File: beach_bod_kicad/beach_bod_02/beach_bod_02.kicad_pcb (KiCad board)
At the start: 2 copper layers, 78.2 x 29.2 mm, 86 parts, among them J1 Conn_01x01, J3 BNC5-J-P-GN-RA-BH2D, J4 Conn_01x01, J5 USB4085-GF-A_REVA4, J6 USB4085-GF-A_REVA4, Q1 AO3401A, U1 LTC6269, U2 LTC6268, U3 LM7301_SOT23_5

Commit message: Routed beach_bod_02
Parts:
- removed the C18 at (152.7, 113.0)
- removed the C19 at (148.7, 113.0)
- removed the C20 at (144.8, 113.0)
- removed the C21 at (140.8, 113.0)
- removed the R15 at (152.8, 109.6)
- removed the R16 at (148.8, 109.6)
- removed the R17 at (144.8, 109.6)
- removed the R18 at (140.9, 109.6)
- removed the R9 at (115.0, 55.8)
- removed the REF** at (150.9, 91.2) (x2)
- C1: renamed from C2; footprint Capacitor_SMD:C_0805_2012Metric_Pad1.18x1.45mm_HandSolder -> Capacitor_SMD:C_0603_1608Metric_Pad1.08x0.95mm_HandSolder
- C12: renamed from C8; footprint Capacitor_SMD:C_0805_2012Metric_Pad1.18x1.45mm_HandSolder -> Capacitor_SMD:C_0603_1608Metric_Pad1.08x0.95mm_HandSolder
- C13: renamed from C9; footprint Capacitor_SMD:C_0805_2012Metric_Pad1.18x1.45mm_HandSolder -> Capacitor_SMD:C_0603_1608Metric_Pad1.08x0.95mm_HandSolder
- C15: renamed from C13; footprint Capacitor_SMD:C_0805_2012Metric_Pad1.18x1.45mm_HandSolder -> Capacitor_SMD:C_0603_1608Metric_Pad1.08x0.95mm_HandSolder
- C16: renamed from C14; footprint Capacitor_SMD:C_0805_2012Metric_Pad1.18x1.45mm_HandSolder -> Capacitor_SMD:C_0603_1608Metric_Pad1.08x0.95mm_HandSolder
- C2: renamed from C3; footprint Capacitor_SMD:C_0805_2012Metric_Pad1.18x1.45mm_HandSolder -> Capacitor_SMD:C_0603_1608Metric_Pad1.08x0.95mm_HandSolder
- C3: renamed from C4; footprint Capacitor_SMD:C_0805_2012Metric_Pad1.18x1.45mm_HandSolder -> Capacitor_SMD:C_0603_1608Metric_Pad1.08x0.95mm_HandSolder
- C32: renamed from C34; footprint Capacitor_SMD:C_1210_3225Metric_Pad1.33x2.70mm_HandSolder -> Capacitor_SMD:C_0603_1608Metric_Pad1.08x0.95mm_HandSolder
- C4: renamed from C5; footprint Capacitor_SMD:C_0805_2012Metric_Pad1.18x1.45mm_HandSolder -> Capacitor_SMD:C_0603_1608Metric_Pad1.08x0.95mm_HandSolder
- C5: renamed from C18; footprint Capacitor_SMD:C_0805_2012Metric_Pad1.18x1.45mm_HandSolder -> Capacitor_SMD:C_0603_1608Metric_Pad1.08x0.95mm_HandSolder
- C6: renamed from C19; footprint Capacitor_SMD:C_0805_2012Metric_Pad1.18x1.45mm_HandSolder -> Capacitor_SMD:C_0603_1608Metric_Pad1.08x0.95mm_HandSolder
- C7: renamed from C20; footprint Capacitor_SMD:C_0805_2012Metric_Pad1.18x1.45mm_HandSolder -> Capacitor_SMD:C_0603_1608Metric_Pad1.08x0.95mm_HandSolder
- C8: renamed from C21; footprint Capacitor_SMD:C_0805_2012Metric_Pad1.18x1.45mm_HandSolder -> Capacitor_SMD:C_0603_1608Metric_Pad1.08x0.95mm_HandSolder
- R1: renamed from R3; footprint Resistor_SMD:R_0805_2012Metric_Pad1.20x1.40mm_HandSolder -> Resistor_SMD:R_0603_1608Metric_Pad0.98x0.95mm_HandSolder
- R10: renamed from R18; footprint Resistor_SMD:R_0805_2012Metric_Pad1.20x1.40mm_HandSolder -> Resistor_SMD:R_0603_1608Metric_Pad0.98x0.95mm_HandSolder
- R2: renamed from R4; footprint Resistor_SMD:R_0805_2012Metric_Pad1.20x1.40mm_HandSolder -> Resistor_SMD:R_0603_1608Metric_Pad0.98x0.95mm_HandSolder
- R3: renamed from R5; footprint Resistor_SMD:R_0805_2012Metric_Pad1.20x1.40mm_HandSolder -> Resistor_SMD:R_0603_1608Metric_Pad0.98x0.95mm_HandSolder
- R4: renamed from R6; footprint Resistor_SMD:R_0805_2012Metric_Pad1.20x1.40mm_HandSolder -> Resistor_SMD:R_0603_1608Metric_Pad0.98x0.95mm_HandSolder
- R5: renamed from R8; footprint Resistor_SMD:R_0805_2012Metric_Pad1.20x1.40mm_HandSolder -> Resistor_SMD:R_0603_1608Metric_Pad0.98x0.95mm_HandSolder
- R6: renamed from R13; footprint Resistor_SMD:R_0805_2012Metric_Pad1.20x1.40mm_HandSolder -> Resistor_SMD:R_0603_1608Metric_Pad0.98x0.95mm_HandSolder
- R7: renamed from R15; footprint Resistor_SMD:R_0805_2012Metric_Pad1.20x1.40mm_HandSolder -> Resistor_SMD:R_0603_1608Metric_Pad0.98x0.95mm_HandSolder
- R8: renamed from R16; footprint Resistor_SMD:R_0805_2012Metric_Pad1.20x1.40mm_HandSolder -> Resistor_SMD:R_0603_1608Metric_Pad0.98x0.95mm_HandSolder
- R9: renamed from R17; footprint Resistor_SMD:R_0805_2012Metric_Pad1.20x1.40mm_HandSolder -> Resistor_SMD:R_0603_1608Metric_Pad0.98x0.95mm_HandSolder
- moved C17 57.8 mm to (115.1, 99.9), turned to 90 degrees
- moved U2 52.0 mm to (115.4, 95.5), turned to 90 degrees
- moved C18 50.7 mm to (116.8, 100.0), turned to 90 degrees
- moved D1 50.3 mm to (141.2, 91.4), turned to -90 degrees
- moved R17 48.8 mm to (120.4, 97.3)
- moved R18 48.6 mm to (110.8, 98.4), turned to 90 degrees
- moved C19 48.3 mm to (112.9, 98.6), turned to 90 degrees
- moved R21 46.4 mm to (126.5, 102.1), turned to 0 degrees
- moved C14 46.2 mm to (127.7, 92.2)
- moved D2 46.2 mm to (141.2, 100.4), turned to 90 degrees
- moved C11 45.4 mm to (112.0, 95.0), turned to 0 degrees
- moved R19 44.4 mm to (134.4, 99.3)
- moved C21 44.4 mm to (121.8, 94.0)
- moved R20 44.3 mm to (122.2, 100.8), turned to 0 degrees
- moved R11 44.3 mm to (134.4, 92.5)
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- renumbered C6 to C10, C7 to C11, C12 to C14, C16 to C17, C17 to C18, C22 to C19, C23 to C20, C24 to C21, C25 to C22, C26 to C23, C27 to C24, C28 to C25, C29 to C26, C30 to C27, C31 to C28, C32 to C29, C33 to C30, C10 to C31, C1 to C9, J3 to J2, J4 to J3, J5 to J4, J6 to J5, R1 to R11, R2 to R12, R7 to R13, R11 to R15, R12 to R16, R14 to R17, R19 to R18, R20 to R19, R21 to R20, R22 to R21, R23 to R22, R25 to R23, R27 to R24, R28 to R25
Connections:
- C12 pad 1: Net-(C13-Pad2) -> GNDREF
- C13 pad 1: Net-(C13-Pad2) -> GNDREF
- C15 pad 2: Net-(C13-Pad2) -> GNDREF
- C16 pad 2: Net-(C13-Pad2) -> GNDREF
- R5 pad 1: Net-(C13-Pad2) -> GNDREF
- R6 pad 2: Net-(C13-Pad2) -> GNDREF
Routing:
- net greg: track 0.00 -> 65.3 mm, vias 7 -> 27
- net Net-(C15-Pad1): track 0.00 -> 38.5 mm
- net V+: track 0.00 -> 36.0 mm
- net Net-(C4-Pad1): track 0.00 -> 33.0 mm
- net cc1: track 0.00 -> 26.7 mm, vias 0 -> 1
- net VCC: track 5.18 -> 31.7 mm, vias 0 -> 8
- net cc2: track 0.00 -> 17.3 mm, vias 0 -> 1
- net Net-(C19-Pad2): track 0.00 -> 14.2 mm
- net Net-(J2-Pad1): track 0.00 -> 13.1 mm
- net V-: track 4.88 -> 16.3 mm, vias 1 -> 2
- net Net-(R17-Pad2): track 0.00 -> 11.0 mm
- net Net-(C1-Pad2): track 0.00 -> 9.48 mm
- net Net-(C5-Pad1): track 0.00 -> 9.10 mm
- net Net-(C14-Pad1): track 0.00 -> 8.87 mm
- net Net-(C14-Pad2): track 0.00 -> 8.42 mm
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- added copper zone on B.Cu, net GNDREF
- added copper zone on F.Cu, net V-
- added copper zone on B.Cu, net VCC

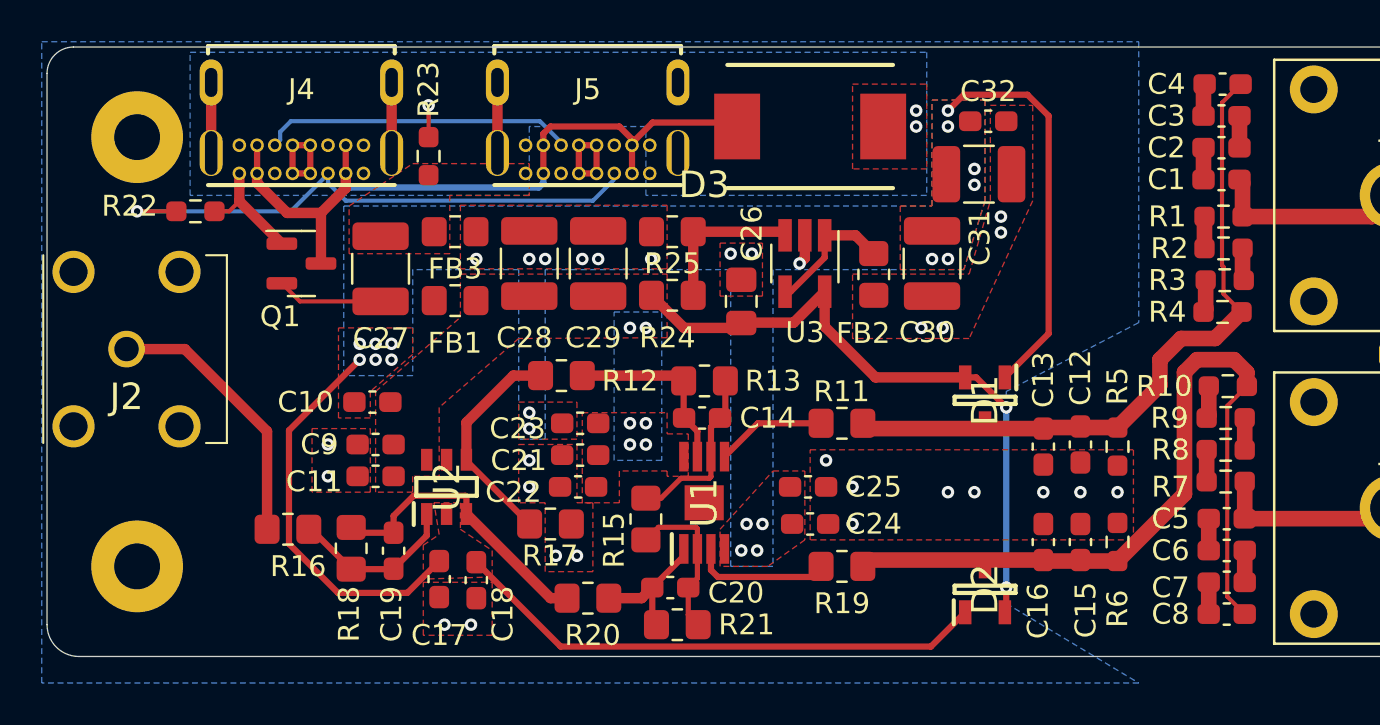
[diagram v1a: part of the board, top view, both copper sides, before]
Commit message: Version saving, added trimpot & BOM
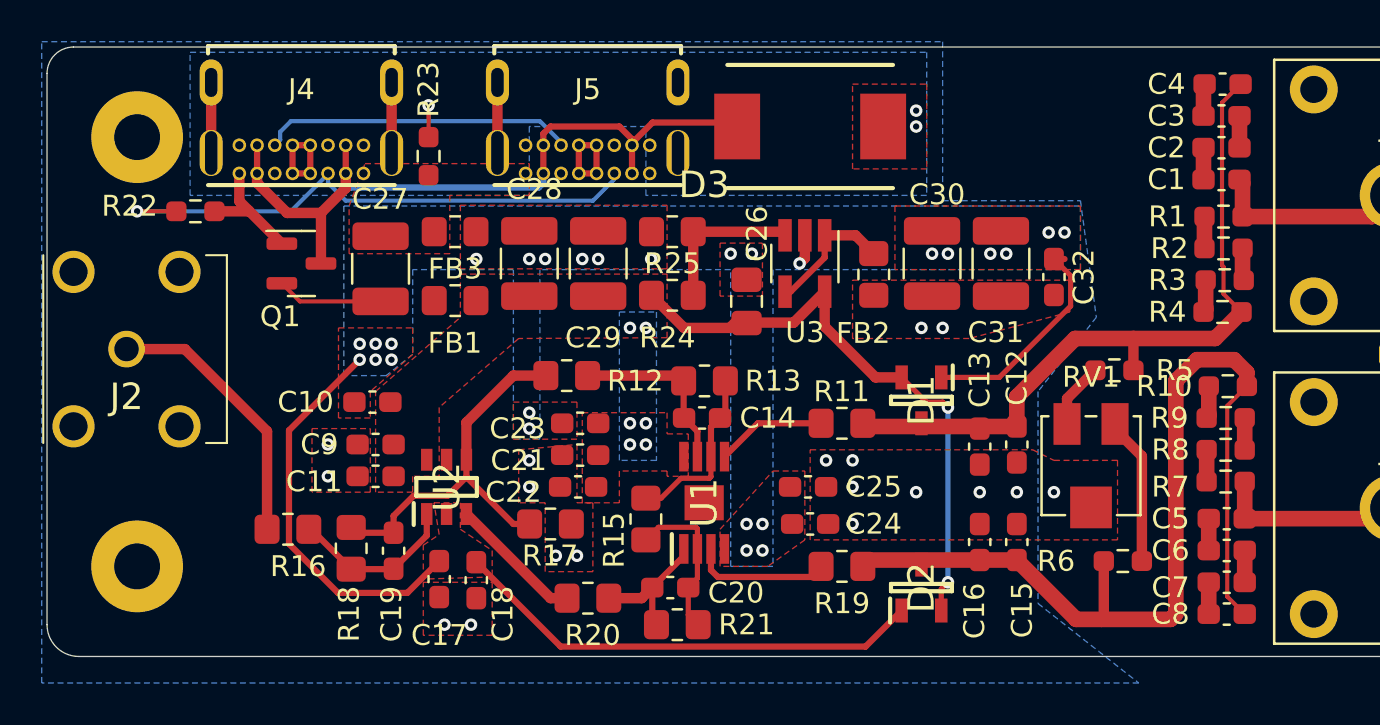
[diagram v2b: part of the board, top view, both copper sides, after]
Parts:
- added RV1: 2k, Potentiometer_SMD:Potentiometer_Bourns_3314J_Vertical, F.Cu at (146.3, 94.5)
- C10, C23: value ~ -> 4.7u
- C11, C18, C22, C24: value ~ -> 100p
- C14, C20: value ~ -> 0.2p +/- 0.05p
- C17, C21, C25, C26, C9: value ~ -> 100n
- C19: value ~ -> 0.4p +/- 0.05p
- C27, C28, C30: value 10u -> 10u tantalum
- R11, R19: value ~ -> 1.5k
- R12, R20: value ~ -> 1.02k 0.1%
- R13, R21: value ~ -> 3.92k
- R15: value ~ -> 412
- R16: value ~ -> 51
- R17, R18: value ~ -> 1.27k 0.1%
- R24, R25: value ~ -> 10k
- moved C32 8.10 mm to (144.5, 85.4), turned to -90 degrees
- moved C31 4.41 mm to (142.0, 84.8), turned to -90 degrees
- moved R5 3.66 mm to (147.4, 89.9), turned to 0 degrees
- moved D2 3.05 mm to (138.2, 100.3)
- moved C12 3.05 mm to (142.7, 93.5)
- moved C13 3.05 mm to (141.0, 93.6)
- moved C15 3.05 mm to (142.7, 98.1)
- moved C16 3.05 mm to (141.0, 98.1)
- moved D1 3.05 mm to (138.2, 91.4)
- moved R6 0.95 mm to (147.8, 99.1), turned to 0 degrees
- moved C26 0.25 mm to (129.8, 86.6)
- moved R12 0.25 mm to (121.2, 90.2)
- turned C27 to 90 degrees
- turned C28 to 90 degrees
- turned C30 to 90 degrees
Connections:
- C27 pad 1: V- -> Net-(FB1-Pad2)
- C27 pad 2: Net-(C27-Pad2) -> V-
- C28 pad 1: greg -> VCC
- C28 pad 2: VCC -> greg
- C30 pad 1: greg -> GNDREF
- C30 pad 2: GNDREF -> greg
- FB1 pad 2: Net-(C27-Pad2) -> Net-(FB1-Pad2)
- Q1 pad 2: Net-(C27-Pad2) -> Net-(FB1-Pad2)
- R12 pad 1: Net-(R17-Pad2) -> Net-(C19-Pad2)
- R17 pad 2: Net-(R17-Pad2) -> Net-(C19-Pad2)
- R20 pad 1: Net-(C19-Pad2) -> Net-(R20-Pad1)
- R5 pad 1: GNDREF -> Net-(R5-Pad1)
- R6 pad 2: GNDREF -> Net-(R6-Pad2)
- U2 pad 3: Net-(C19-Pad2) -> Net-(R20-Pad1)
- U2 pad 4: Net-(R17-Pad2) -> Net-(C19-Pad2)
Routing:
- net greg: track 65.3 -> 54.1 mm
- net Net-(R17-Pad2): track 11.0 -> 0.00 mm
- net Net-(C15-Pad1): track 38.5 -> 46.8 mm
- net Net-(R6-Pad2): track 0.00 -> 7.21 mm
- net Net-(R20-Pad1): track 0.00 -> 6.49 mm
- net Net-(FB1-Pad2): track 0.00 -> 5.09 mm
- net Net-(C27-Pad2): track 5.09 -> 0.00 mm
- net Net-(C19-Pad2): track 14.2 -> 18.3 mm
- net Net-(R5-Pad1): track 0.00 -> 3.13 mm
- net VCC: track 31.7 -> 29.0 mm
- net Net-(C12-Pad2): track 33.0 -> 34.9 mm
- net GNDREF: vias 20 -> 18
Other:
- board text added: "beach_bod_v02 jan2023 //keyudits"
- board text removed: "beach_bod_v01 Nov2022 //keyudits"

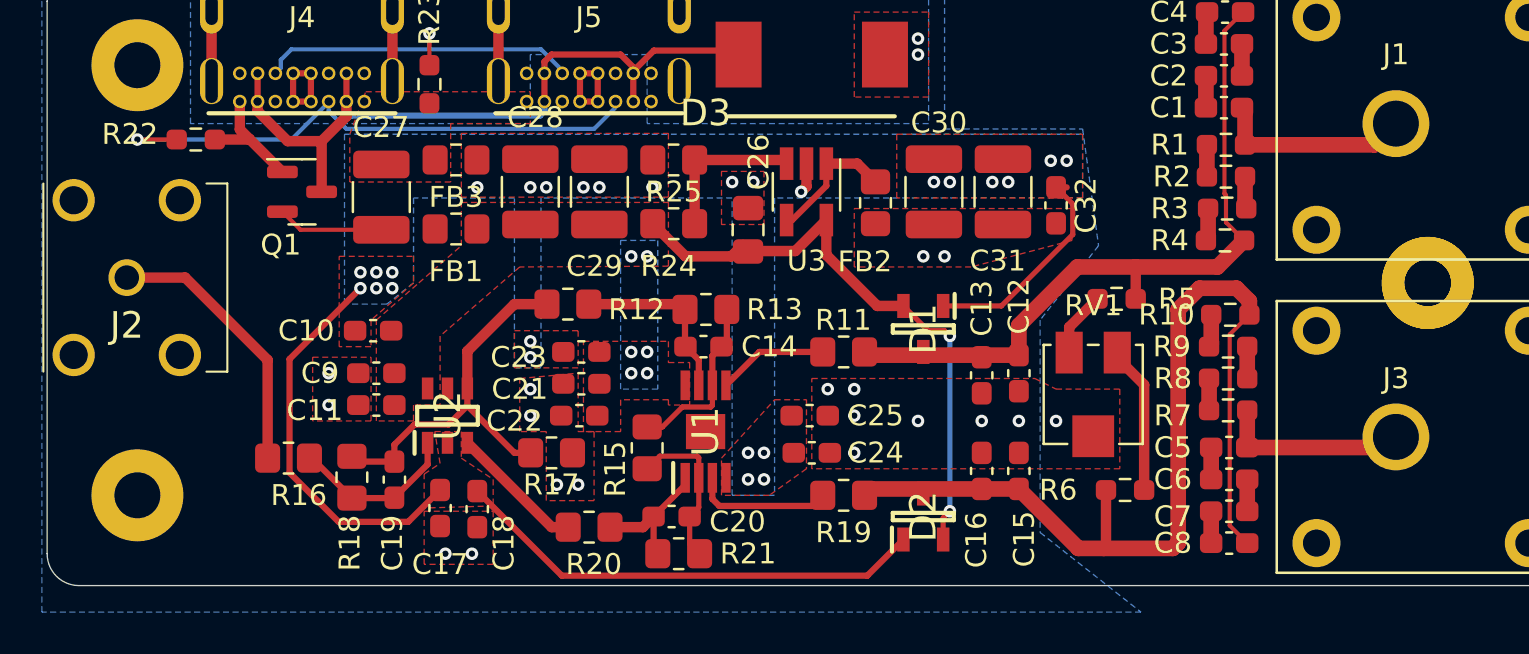
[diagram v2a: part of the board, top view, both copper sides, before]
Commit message: Added beach_bod_v02_cart
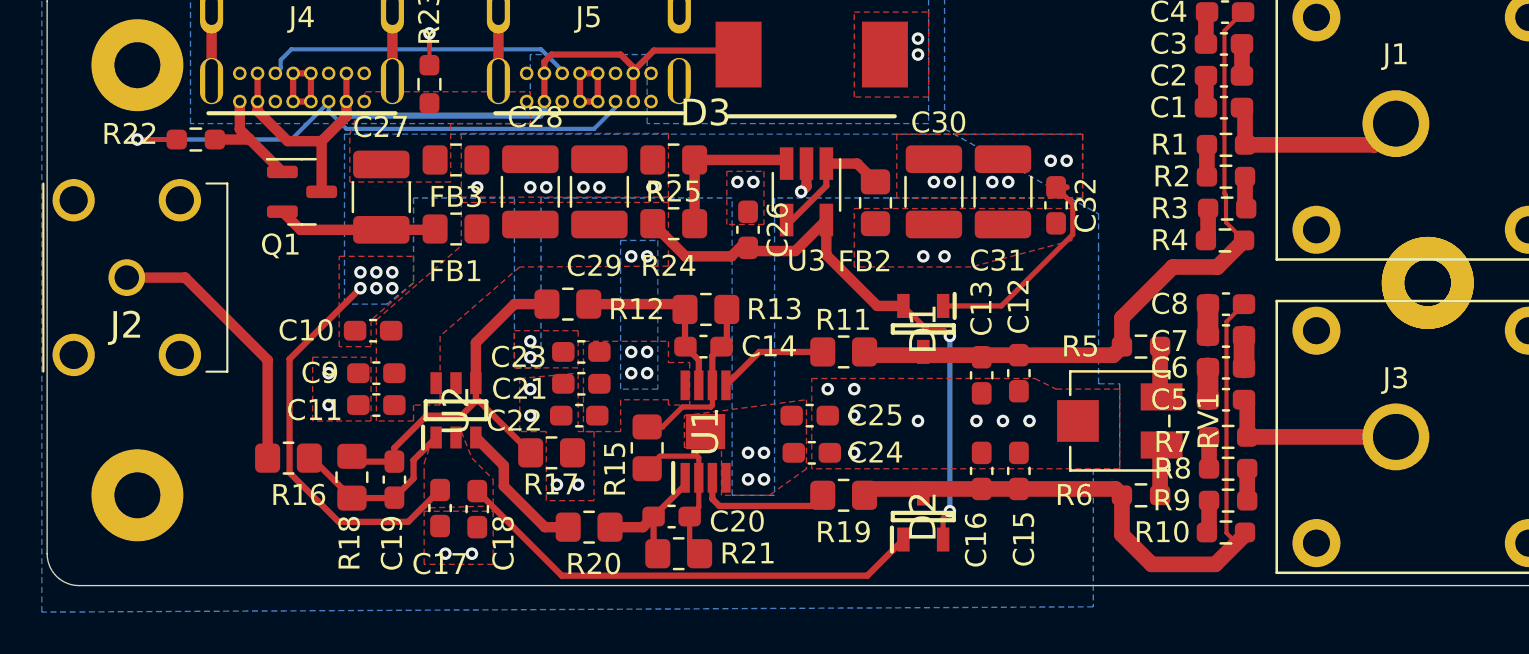
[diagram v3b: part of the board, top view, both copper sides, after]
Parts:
- C26: footprint Capacitor_SMD:C_0805_2012Metric_Pad1.18x1.45mm_HandSolder -> Capacitor_SMD:C_0603_1608Metric_Pad1.08x0.95mm_HandSolder
- moved C8 11.4 mm to (152.7, 90.2)
- moved R10 10.4 mm to (152.7, 101.1)
- moved C7 8.38 mm to (152.7, 91.7)
- moved R9 7.37 mm to (152.8, 99.6)
- moved C6 5.34 mm to (152.7, 93.2)
- moved R8 4.32 mm to (152.8, 98.0)
- moved R5 2.57 mm to (148.6, 92.2), turned to 180 degrees
- moved C5 2.29 mm to (152.7, 94.7)
- moved RV1 1.80 mm to (147.6, 95.8), turned to -90 degrees
- moved R7 1.27 mm to (152.8, 96.5)
- moved R6 0.80 mm to (148.6, 99.3)
- moved U2 0.48 mm to (115.8, 95.2)
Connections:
- net Net-(C12-Pad2) renamed sig_P
- net Net-(C15-Pad1) renamed sig_N
- U1 pad 9: (no net) -> greg
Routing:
- net sig_N: track 46.8 -> 33.6 mm
- net Net-(R6-Pad2): track 7.21 -> 2.44 mm
- net Net-(FB1-Pad2): track 5.09 -> 7.68 mm
- net sig_P: track 34.9 -> 33.3 mm
- net Net-(R5-Pad1): track 3.13 -> 2.44 mm
- net Net-(C5-Pad1): track 9.10 -> 9.67 mm

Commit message: Added v02 gerbers & testing notes
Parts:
- removed ?: , 
- added gnd: PinHeader_1x01_P2.54mm_Vertical, Connector_PinHeader_2.54mm:PinHeader_1x01_P2.54mm_Vertical, F.Cu at (137.2, 96.0)
- added greg: PinHeader_1x01_P2.54mm_Vertical, Connector_PinHeader_2.54mm:PinHeader_1x01_P2.54mm_Vertical, F.Cu at (131.1, 90.4)
- added sig+: PinHeader_1x01_P2.54mm_Vertical, Connector_PinHeader_2.54mm:PinHeader_1x01_P2.54mm_Vertical, F.Cu at (148.1, 89.9)
- added sig-: PinHeader_1x01_P2.54mm_Vertical, Connector_PinHeader_2.54mm:PinHeader_1x01_P2.54mm_Vertical, F.Cu at (148.1, 101.9)
- added vcc: PinHeader_1x01_P2.54mm_Vertical, Connector_PinHeader_2.54mm:PinHeader_1x01_P2.54mm_Vertical, F.Cu at (115.6, 90.2)
- moved R5 0.25 mm to (148.6, 92.5)
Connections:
- U1 pad 9: greg -> (no net)
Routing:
- net Net-(C5-Pad1): track 9.67 -> 8.95 mm
- net Net-(C20-Pad1): track 6.63 -> 6.01 mm
- net V-: track 16.5 -> 16.0 mm
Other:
- rule pad_to_mask_clearance: 0.05 -> 0
- board text added: "blk"
- board text added: "ferrite beads were too small for footprint"
- board text added: "red"
- board text added: "shift usbc towards middle"
